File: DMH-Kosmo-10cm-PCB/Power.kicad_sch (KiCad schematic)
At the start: 13 parts, among them J100 IDC_02x08, J101 IDC_02x05

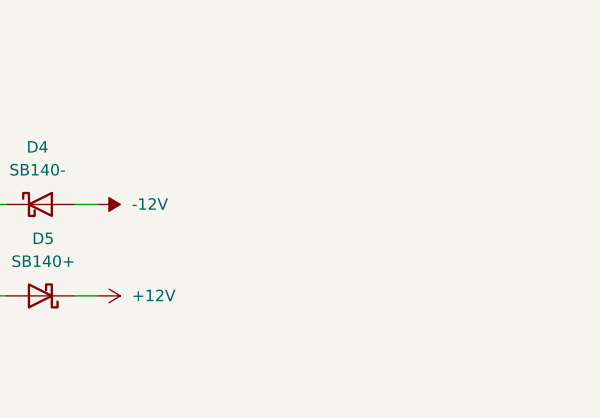
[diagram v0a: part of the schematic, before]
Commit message: Updated 5cm and 10 templates
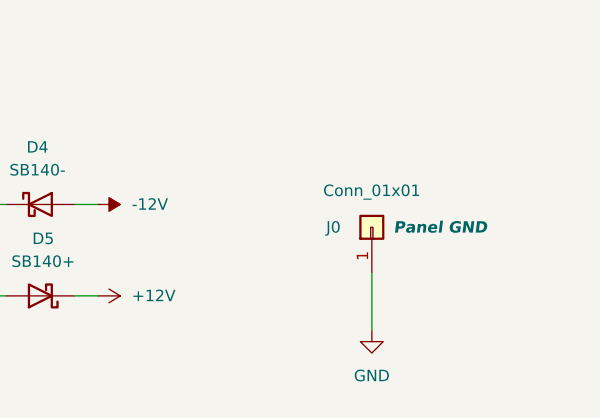
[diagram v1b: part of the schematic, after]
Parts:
- added J0: Conn_01x01, Connector_PinHeader_2.54mm:PinHeader_1x01_P2.54mm_Vertical, symbol Connector_Generic:Conn_01x01
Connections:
- net GND: now also J0.1 (Pin_1)
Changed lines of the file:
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@@
+	(wire
+		(pts
+			(xy 152.4 182.88) (xy 152.4 189.23)
+		)
+		(stroke
+			(width 0)
+			(type default)
+		)
+	)
 	(wire
 		(pts
@@
 					(unit 1)
 				)
+			)
+		)
+	)
+	(symbol
+		(lib_id "power:GND")
+		(at 152.4 189.23 0)
+		(unit 1)
+		(exclude_from_sim no)
+		(in_bom yes)
+		(on_board yes)
+		(dnp no)
+		(fields_autoplaced yes)
+		(property "Reference" "#PWR08"
+			(at 152.4 195.58 0)
+			(effects
+				(font
+					(size 1.27 1.27)
+				)
+				(hide yes)
+			)
+		)
+		(property "Value" "GND"
+			(at 152.4 194.31 0)
+			(effects
+				(font
+					(size 1.27 1.27)
+				)
+			)
+		)
+		(property "Footprint" ""
+			(at 152.4 189.23 0)
+			(effects
+				(font
+					(size 1.27 1.27)
+				)
+				(hide yes)
+			)
+		)
+		(property "Datasheet" ""
+			(at 152.4 189.23 0)
+			(effects
+				(font
+					(size 1.27 1.27)
+				)
+				(hide yes)
+			)
+		)
+		(property "Description" "Power symbol creates a global label with name \"GND\" , ground"
+			(at 152.4 189.23 0)
+			(effects
+				(font
+					(size 1.27 1.27)
+				)
+				(hide yes)
+			)
+		)
+		(pin "1"
+		)
+		(instances
+			(project "DMH-Kosmo-10cm-PCB"
+				(path "/58f4306d-5387-4983-bb08-41a2313fd315/0cdf34b2-39cd-4d9e-981a-97cd34791509"
+					(reference "#PWR08")
+					(unit 1)
+				)
+			)
+		)
+	)
+	(symbol
+		(lib_id "Connector_Generic:Conn_01x01")
+		(at 152.4 177.8 90)
+		(unit 1)
+		(exclude_from_sim no)
+		(in_bom yes)
+		(on_board yes)
+		(dnp no)
+		(property "Reference" "J0"
+			(at 147.32 177.8 90)
+			(effects
+				(font
+					(size 1.27 1.27)
+				)
+				(justify right)
+			)
+		)
+		(property "Value" "Conn_01x01"
+			(at 152.4 173.736 90)
+			(effects
+				(font
+					(size 1.27 1.27)
+				)
+			)
+		)
+		(property "Footprint" "Connector_PinHeader_2.54mm:PinHeader_1x01_P2.54mm_Vertical"
+			(at 152.4 177.8 0)
+			(effects
+				(font
+					(size 1.27 1.27)
+				)
+				(hide yes)
+			)
+		)
+		(property "Datasheet" "~"
+			(at 152.4 177.8 0)
+			(effects
+				(font
+					(size 1.27 1.27)
+				)
+				(hide yes)
+			)
+		)
+		(property "Description" "Generic connector, single row, 01x01, script generated (kicad-library-utils/schlib/autogen/connector/)"
+			(at 152.4 177.8 0)
+			(effects
+				(font
+					(size 1.27 1.27)
+				)
+				(hide yes)
+			)
+		)
+		(property "Function" "Panel GND"
+			(at 160.02 177.8 90)
+			(effects
+				(font
+					(size 1.27 1.27)
+					(thickness 0.254)
+					(bold yes)
+					(italic yes)
+				)
+			)
+		)
+		(pin "1"
+		)
+		(instances
+			(project "DMH-Kosmo-10cm-PCB"
+				(path "/58f4306d-5387-4983-bb08-41a2313fd315/0cdf34b2-39cd-4d9e-981a-97cd34791509"
+					(reference "J0")
+					(unit 1)
+				)

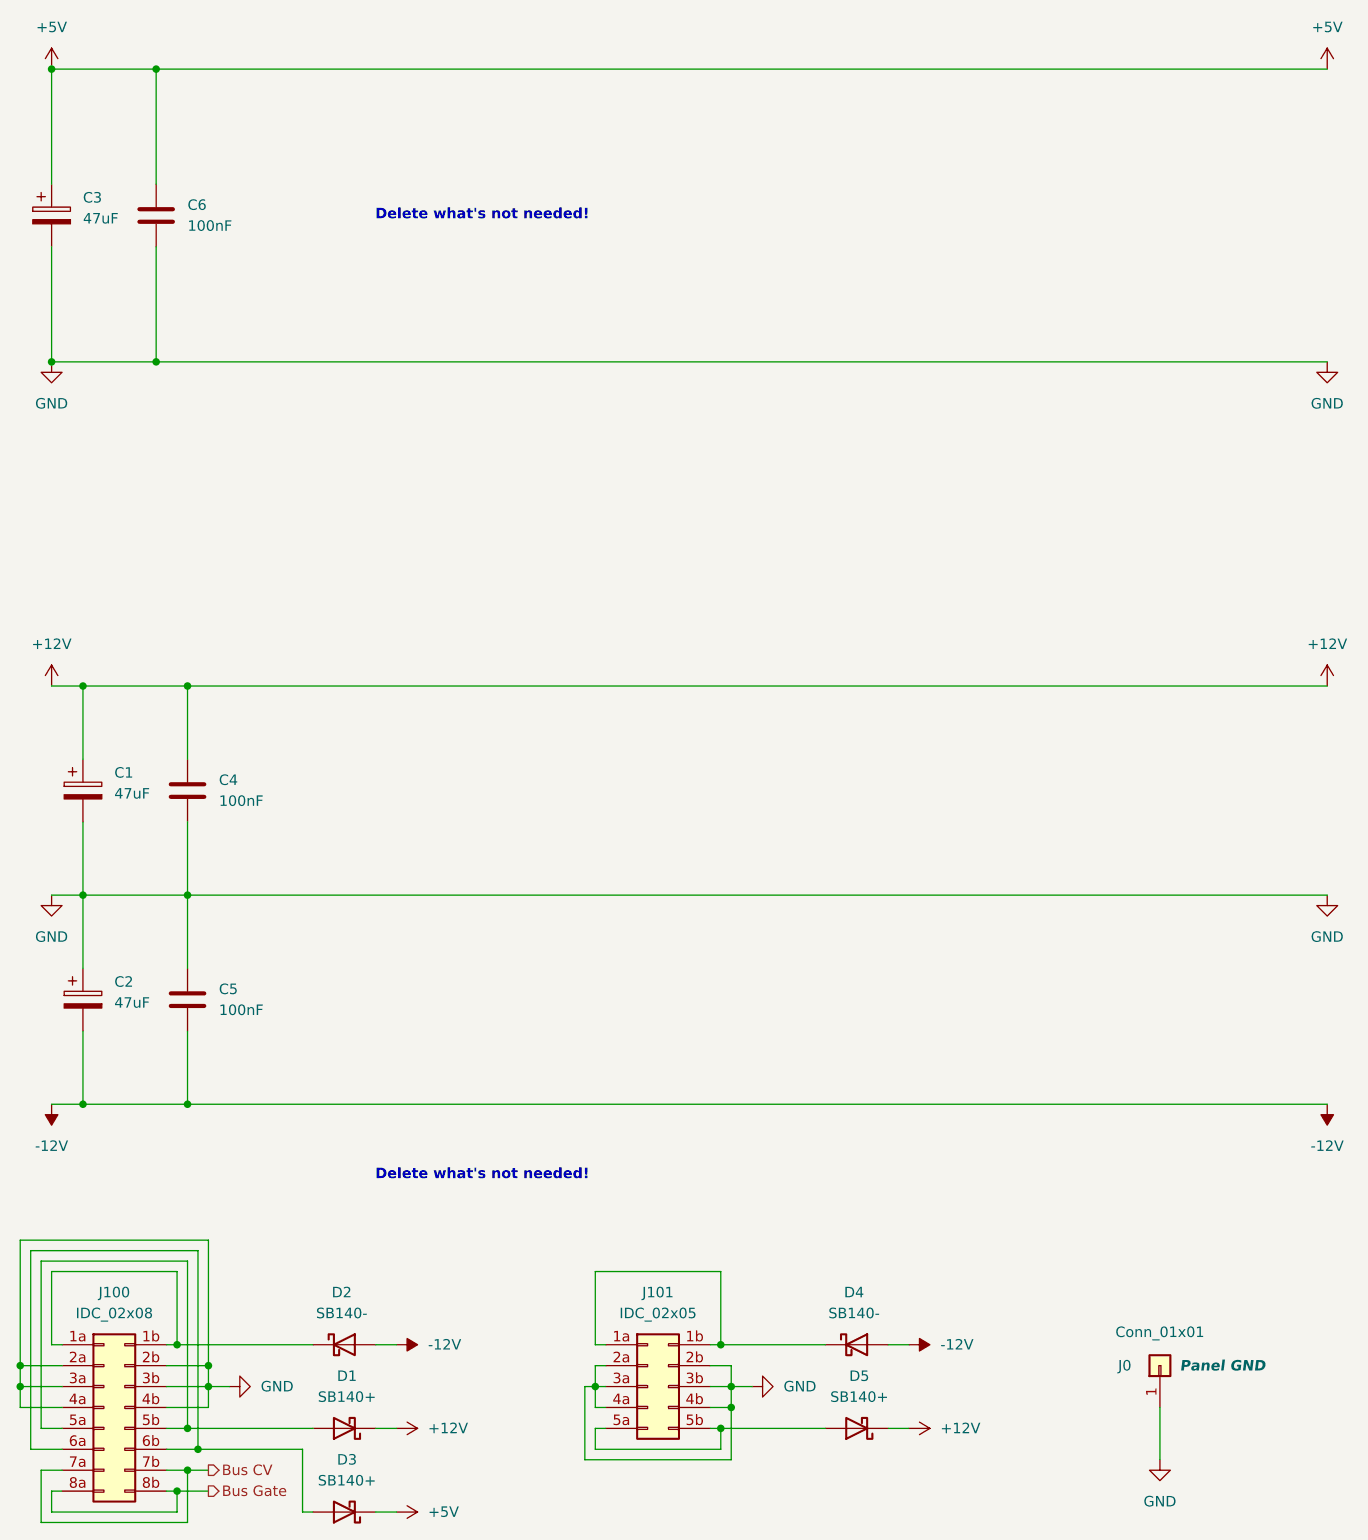
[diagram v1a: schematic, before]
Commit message: Minor fixes on schematic templates
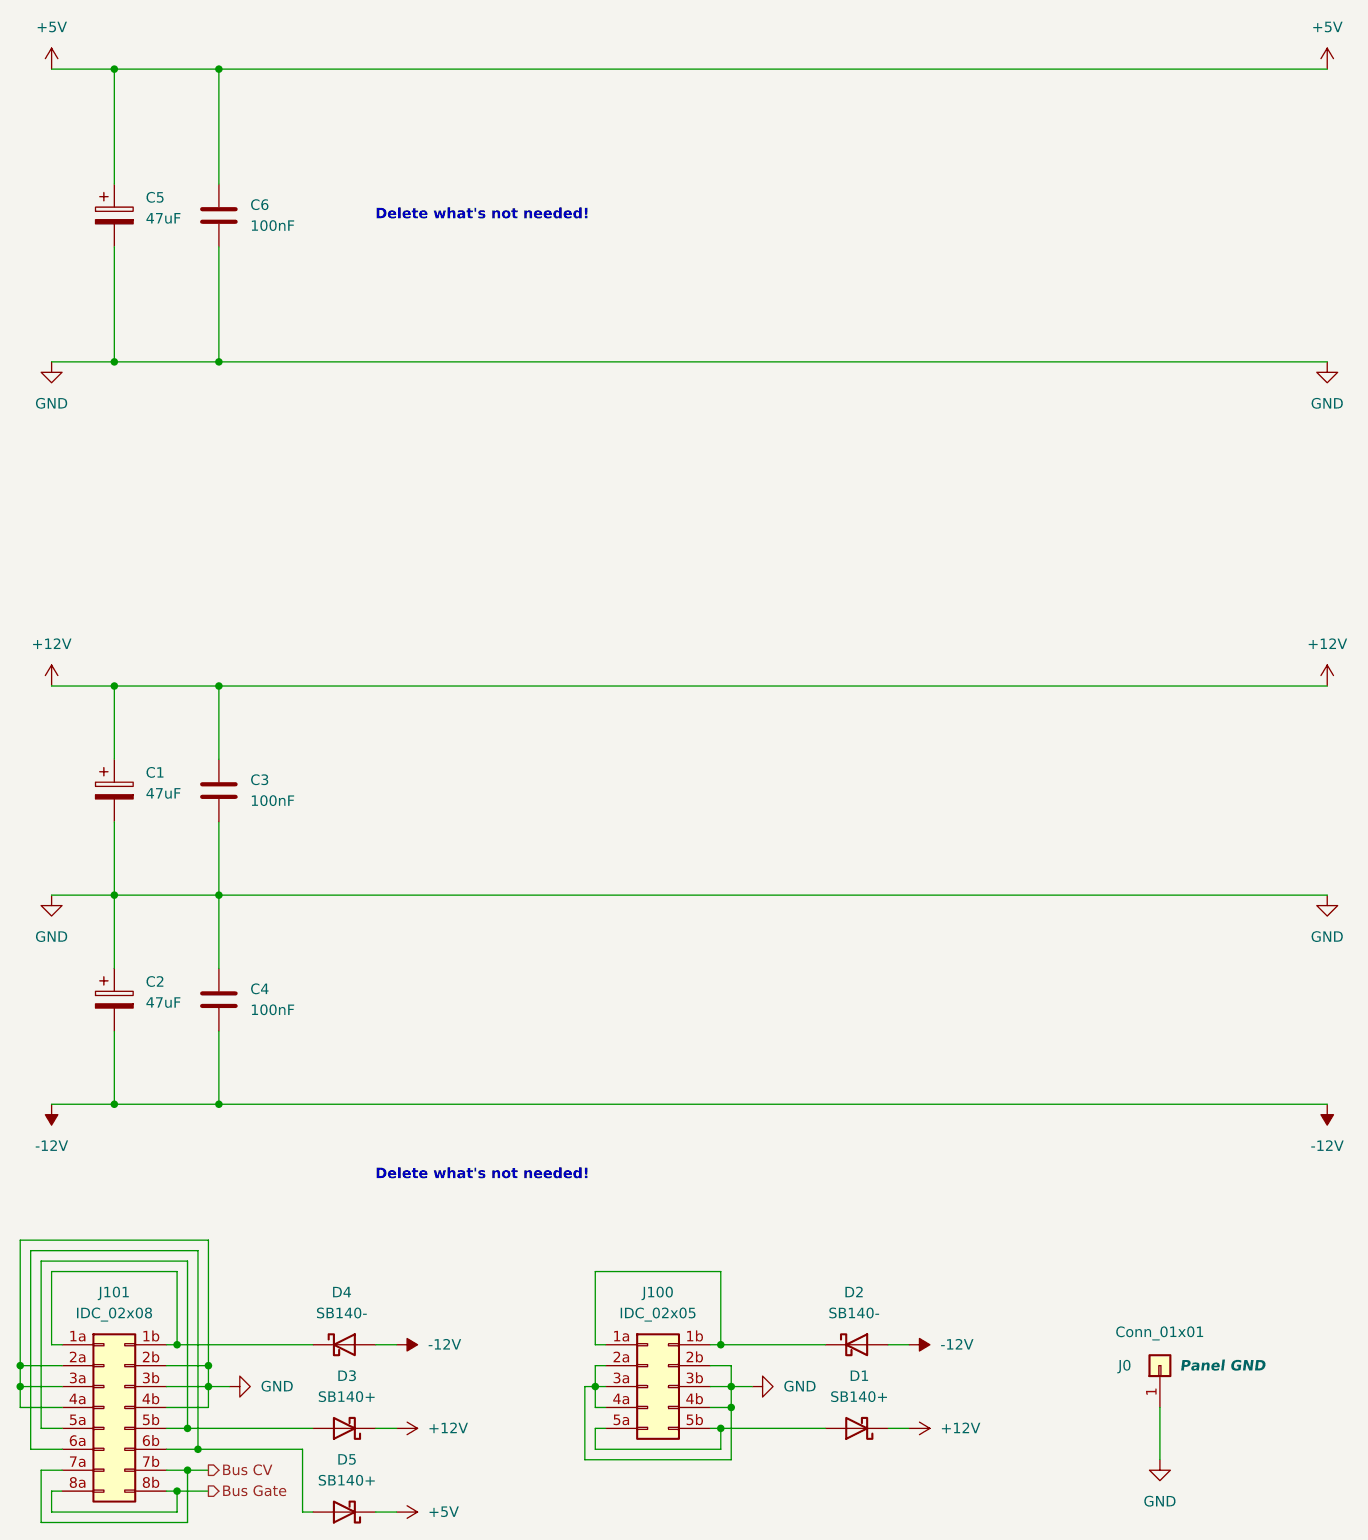
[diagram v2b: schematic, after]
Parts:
- renumbered C4 to C3, C5 to C4, C3 to C5, D5 to D1, D4 to D2, D1 to D3, D2 to D4, D3 to D5, J101 to J100, J100 to J101
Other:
- moved on the sheet: C1, C2, C3, C4, C5, C6

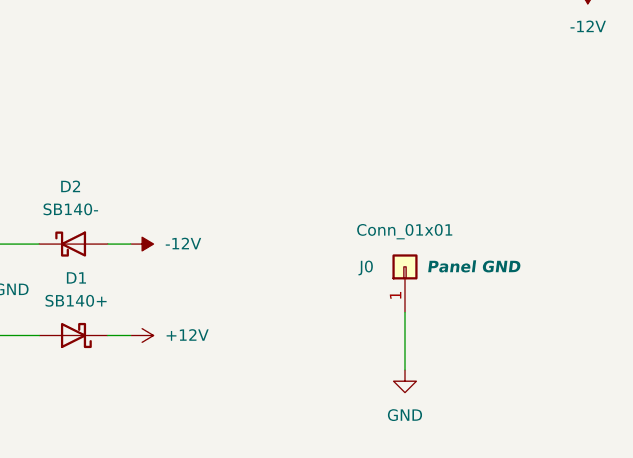
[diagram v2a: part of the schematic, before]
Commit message: Added initial jacks and connectors to PCBs
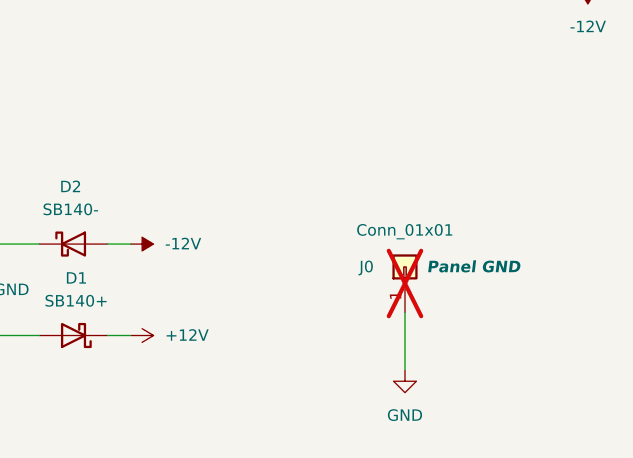
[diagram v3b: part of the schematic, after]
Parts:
- J0: now not fitted; now left out of the parts list
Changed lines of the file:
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@@
 		(unit 1)
 		(exclude_from_sim no)
-		(in_bom yes)
+		(in_bom no)
 		(on_board yes)
-		(dnp no)
+		(dnp yes)
 		(property "Reference" "J0"
 			(at 147.32 177.8 90)

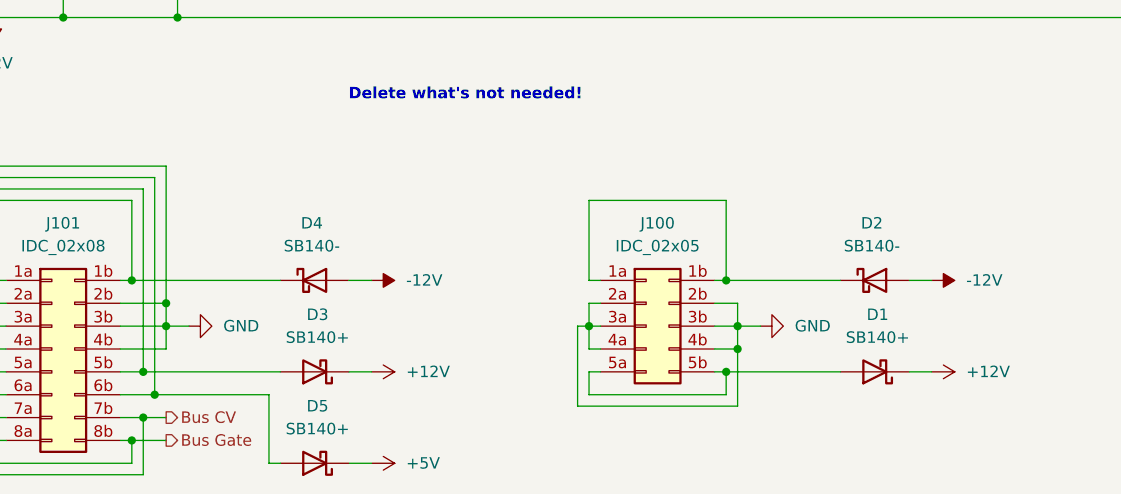
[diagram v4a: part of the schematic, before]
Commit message: Updated schotky diodes on Power sheets
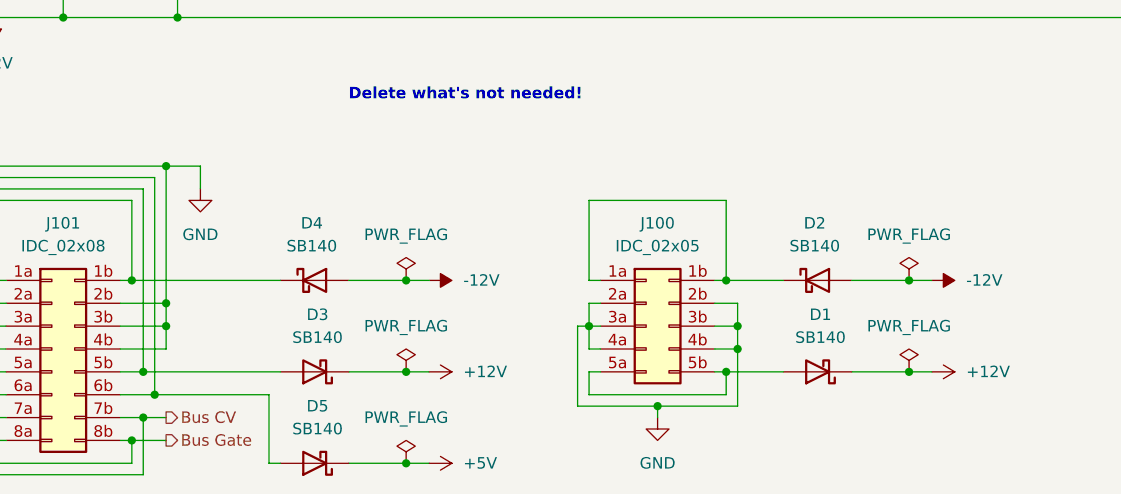
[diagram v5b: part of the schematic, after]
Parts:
- D1, D3, D5: value SB140+ -> SB140; symbol SynthStuff:Power_Bus_Schotty_+ -> Diode:SB140
- D2, D4: value SB140- -> SB140; symbol SynthStuff:Power_Bus_Schotty_- -> Diode:SB140
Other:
- moved on the sheet: D1, D2
